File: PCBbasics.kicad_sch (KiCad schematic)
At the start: 9 parts

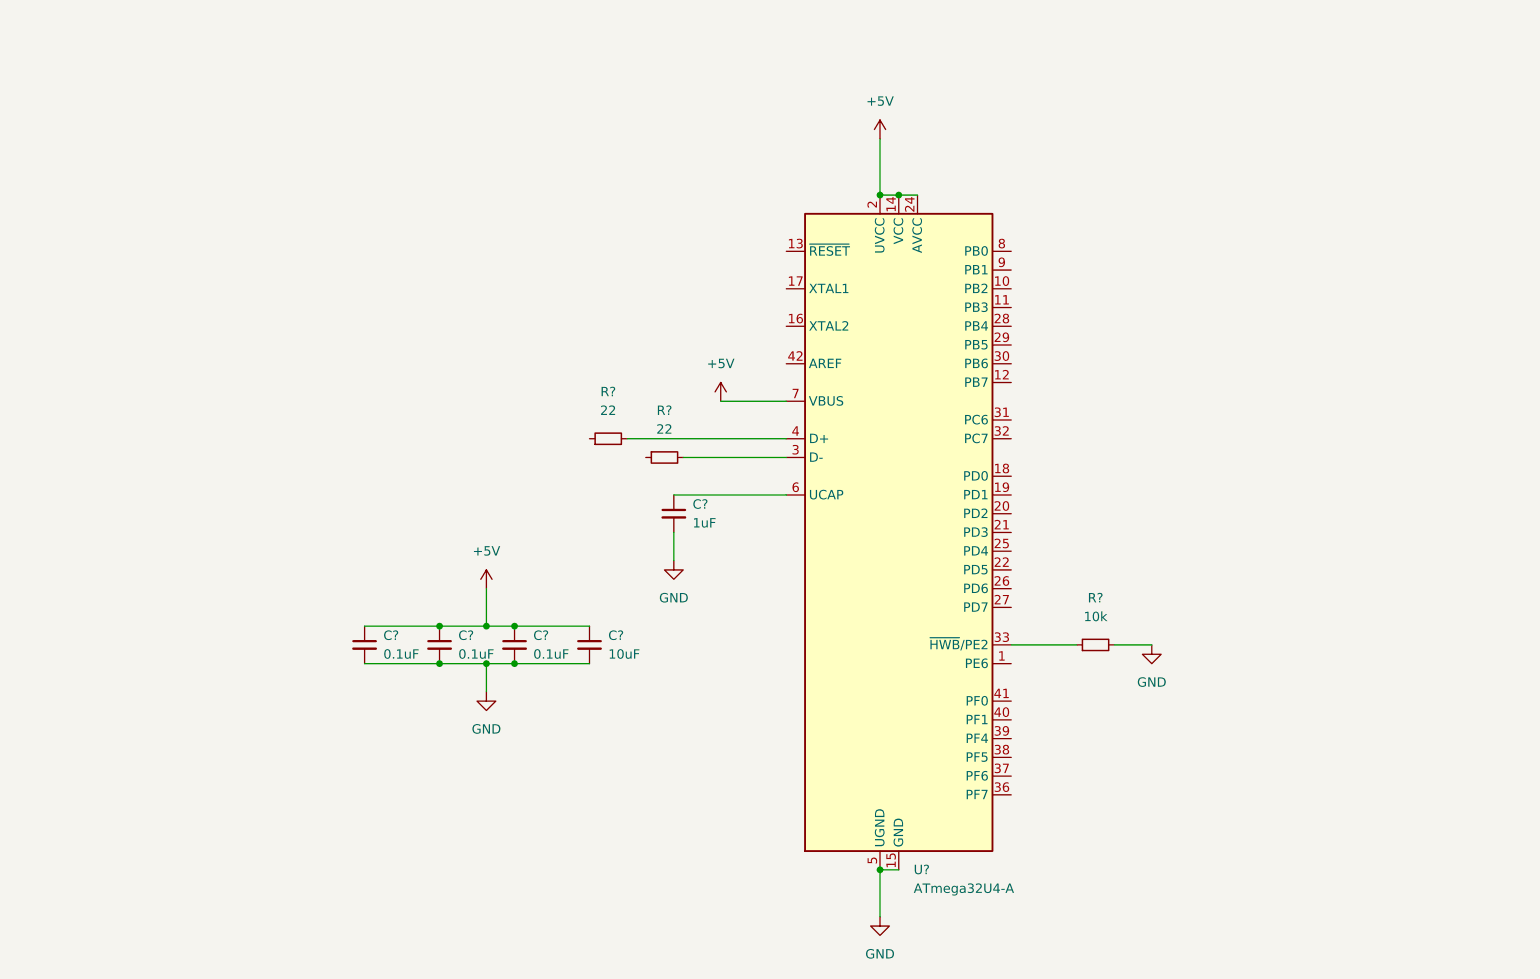
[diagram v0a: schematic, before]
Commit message: Completed MCU Area
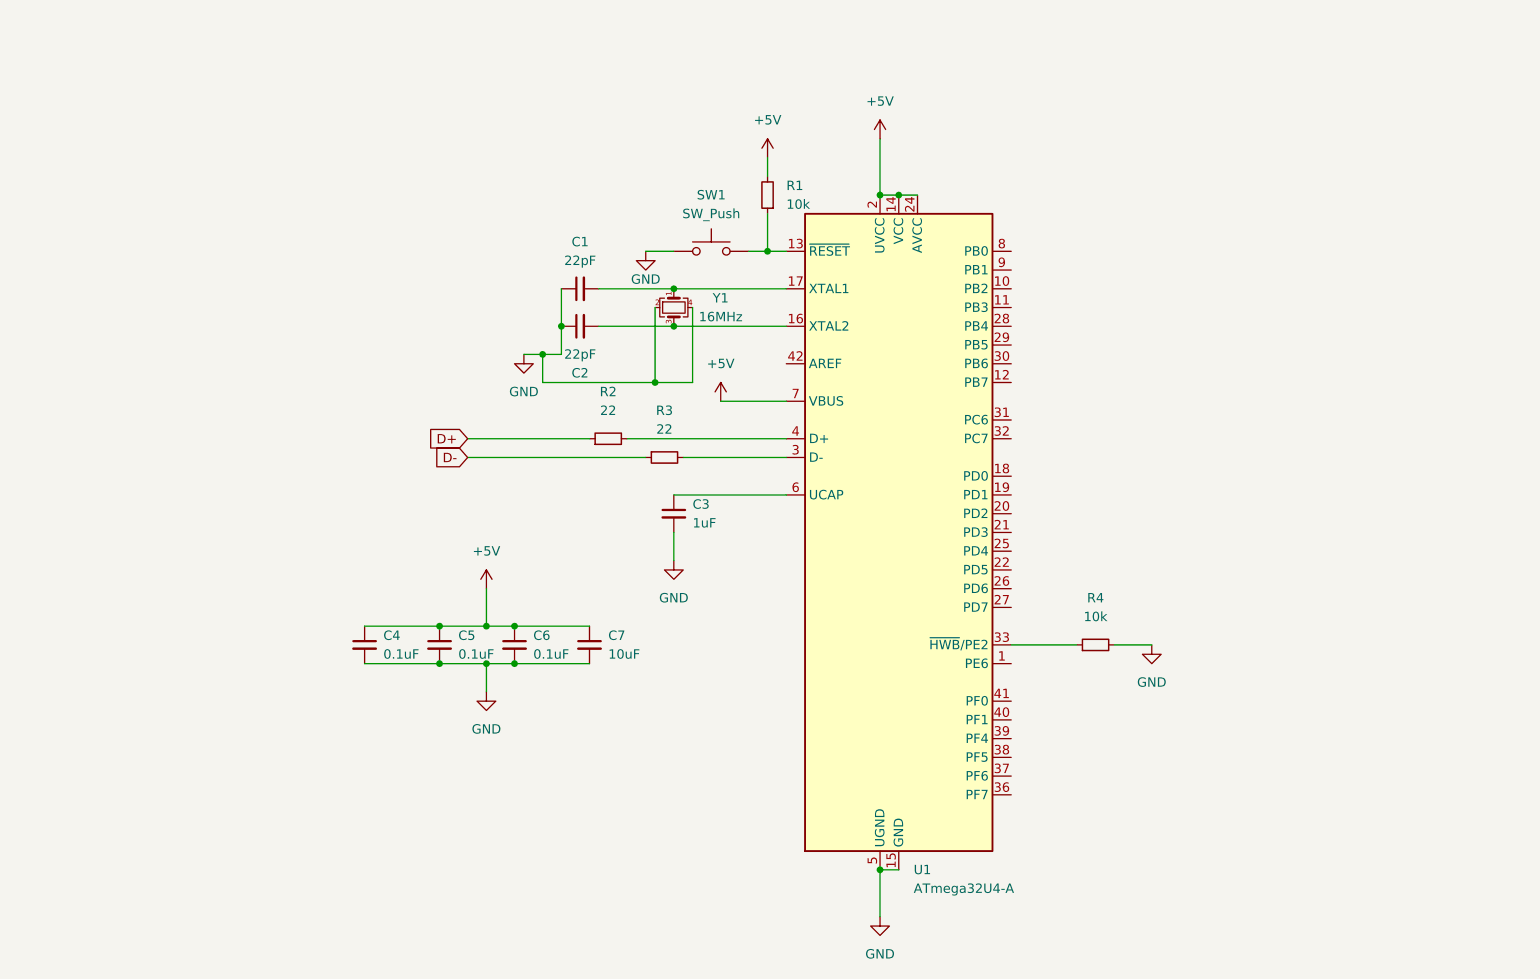
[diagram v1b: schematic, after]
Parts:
- added C1, C2: 22pF, symbol Device:C_Small
- added R1: 10k, symbol Device:R_Small
- added SW1: SW_Push, symbol Switch:SW_Push
- added Y1: 16MHz, symbol Device:Crystal_GND24_Small
- gave numbers to parts that had none: 9
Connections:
- net +5V: now also R1.2
- net GND: now also C1.1, C2.1, SW1.1, Y1.2, Y1.4
- net D-: now reaches R3.1
- net at U1.13 (~{RESET}): now also R1.1, SW1.2
- net at U1.16 (XTAL2): now also C2.2, Y1.3
- net at U1.17 (XTAL1): now also C1.2, Y1.1
- net D+: now reaches R2.1

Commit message: Schematic Done - Micro USB Ver.
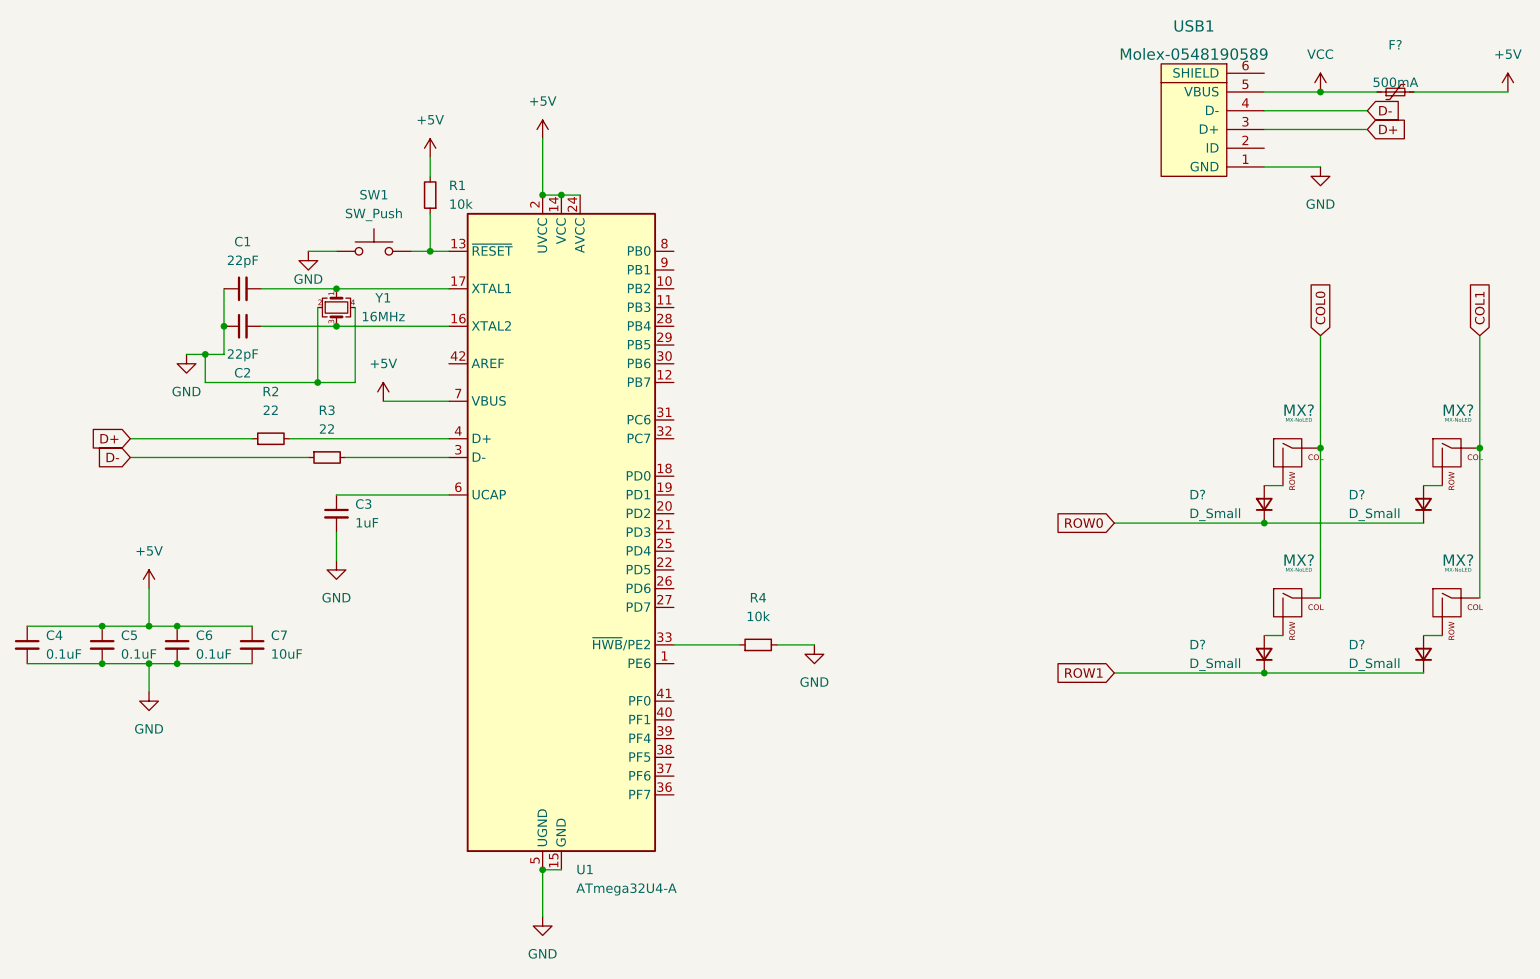
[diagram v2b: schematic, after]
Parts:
- added D? (x4): D_Small, symbol Device:D_Small
- added F?: 500mA, symbol Device:Polyfuse_Small
- added MX? (x4): MX-NoLED, symbol MX_Alps_Hybrid:MX-NoLED
- added USB1: Molex-0548190589, symbol random-keyboard-parts:Molex-0548190589
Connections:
- net +5V: now also F?.2
- net D+: now also USB1.3 (D+)
- net D-: now also USB1.4 (D-)
- net GND: now also USB1.1 (GND)
- new net: D?.2 (A), MX?.2 (ROW) (x4)
- new net COL0: MX?.1 (COL), MX?.1 (COL)
- new net COL1: MX?.1 (COL), MX?.1 (COL)
- new net ROW0: D?.1 (K), D?.1 (K)
- new net ROW1: D?.1 (K), D?.1 (K)
- new net VCC: F?.1, USB1.5 (VBUS)
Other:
- moved on the sheet: C1, C2, C3, C4, C5, C6, C7, R1, R2, R3, R4, SW1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

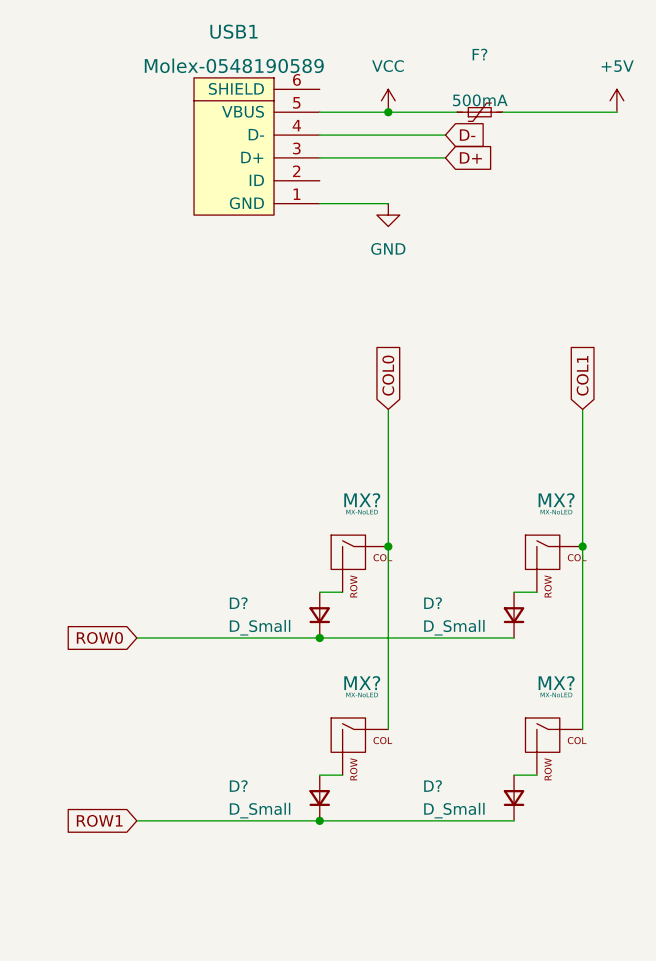
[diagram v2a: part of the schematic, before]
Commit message: Footprints annotated
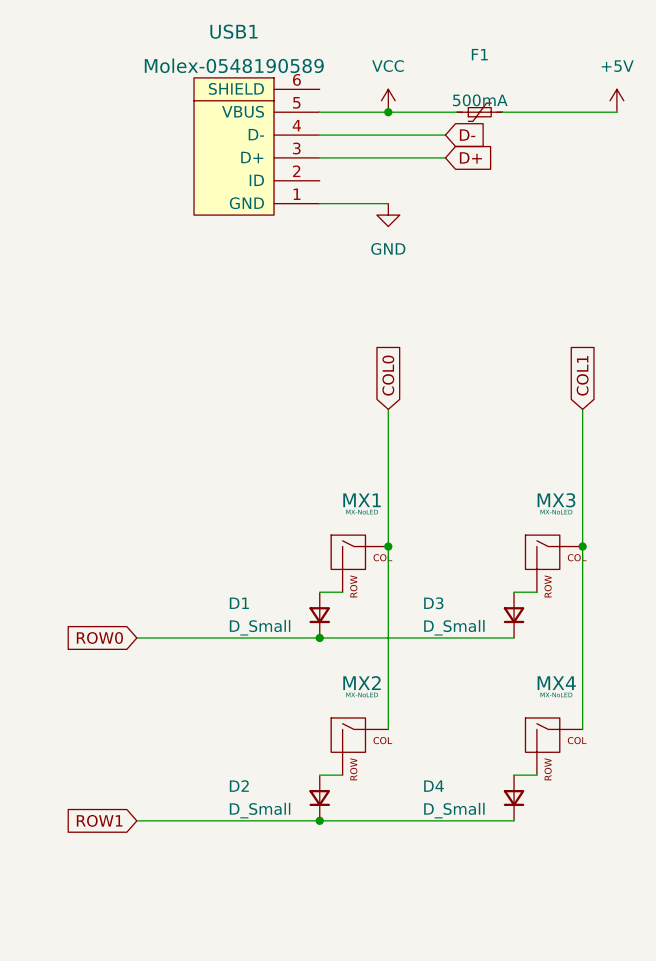
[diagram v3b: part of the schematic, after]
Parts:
- C1, C2, C3, C4, C5, C6, C7: footprint (none) -> Capacitor_SMD:C_0805_2012Metric
- D1, D2, D3, D4: renamed from D?; footprint (none) -> Diode_SMD:D_SOD-123
- F1: renamed from F?; footprint (none) -> Fuse:Fuse_1206_3216Metric
- MX1, MX2, MX3, MX4: renamed from MX?; footprint (none) -> MX_Alps_Hybrid:MX-1U-NoLED
- R1, R2, R3, R4: footprint (none) -> Resistor_SMD:R_0805_2012Metric_Pad1.20x1.40mm_HandSolder
- SW1: footprint (none) -> random-keyboard-parts:SKQG-1155865
- USB1: footprint (none) -> random-keyboard-parts:PJ-3200B-4A-Assembly
- Y1: footprint (none) -> Crystal:Crystal_SMD_3225-4Pin_3.2x2.5mm

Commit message: PCB Finished
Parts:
- USB1: footprint random-keyboard-parts:PJ-3200B-4A-Assembly -> random-keyboard-parts:Molex-0548190589
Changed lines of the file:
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@@
       (effects (font (size 1.524 1.524)))
     )
-    (property "Footprint" "random-keyboard-parts:PJ-3200B-4A-Assembly" (id 2) (at 177.8 39.37 0)
+    (property "Footprint" "random-keyboard-parts:Molex-0548190589" (id 2) (at 177.8 39.37 0)
       (effects (font (size 1.524 1.524)) hide)
     )
@@
     )
     (path "/c41edebf-027b-45ad-aedd-a14fe23f799f"
-      (reference "USB1") (unit 1) (value "Molex-0548190589") (footprint "random-keyboard-parts:PJ-3200B-4A-Assembly")
+      (reference "USB1") (unit 1) (value "Molex-0548190589") (footprint "random-keyboard-parts:Molex-0548190589")
     )
     (path "/1d584bc5-6840-4f20-bf2e-c93acd3b95ea"
